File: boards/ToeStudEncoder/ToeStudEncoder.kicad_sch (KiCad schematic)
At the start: 23 parts, among them J1 Swell, J2 ISP, J3 ToeLeft, J4 ToeRight, J5 MIDI In, J6 Controller, J7 Pedal, J8 MIDI Out, U1 ATmega48-20P, U2 6N138

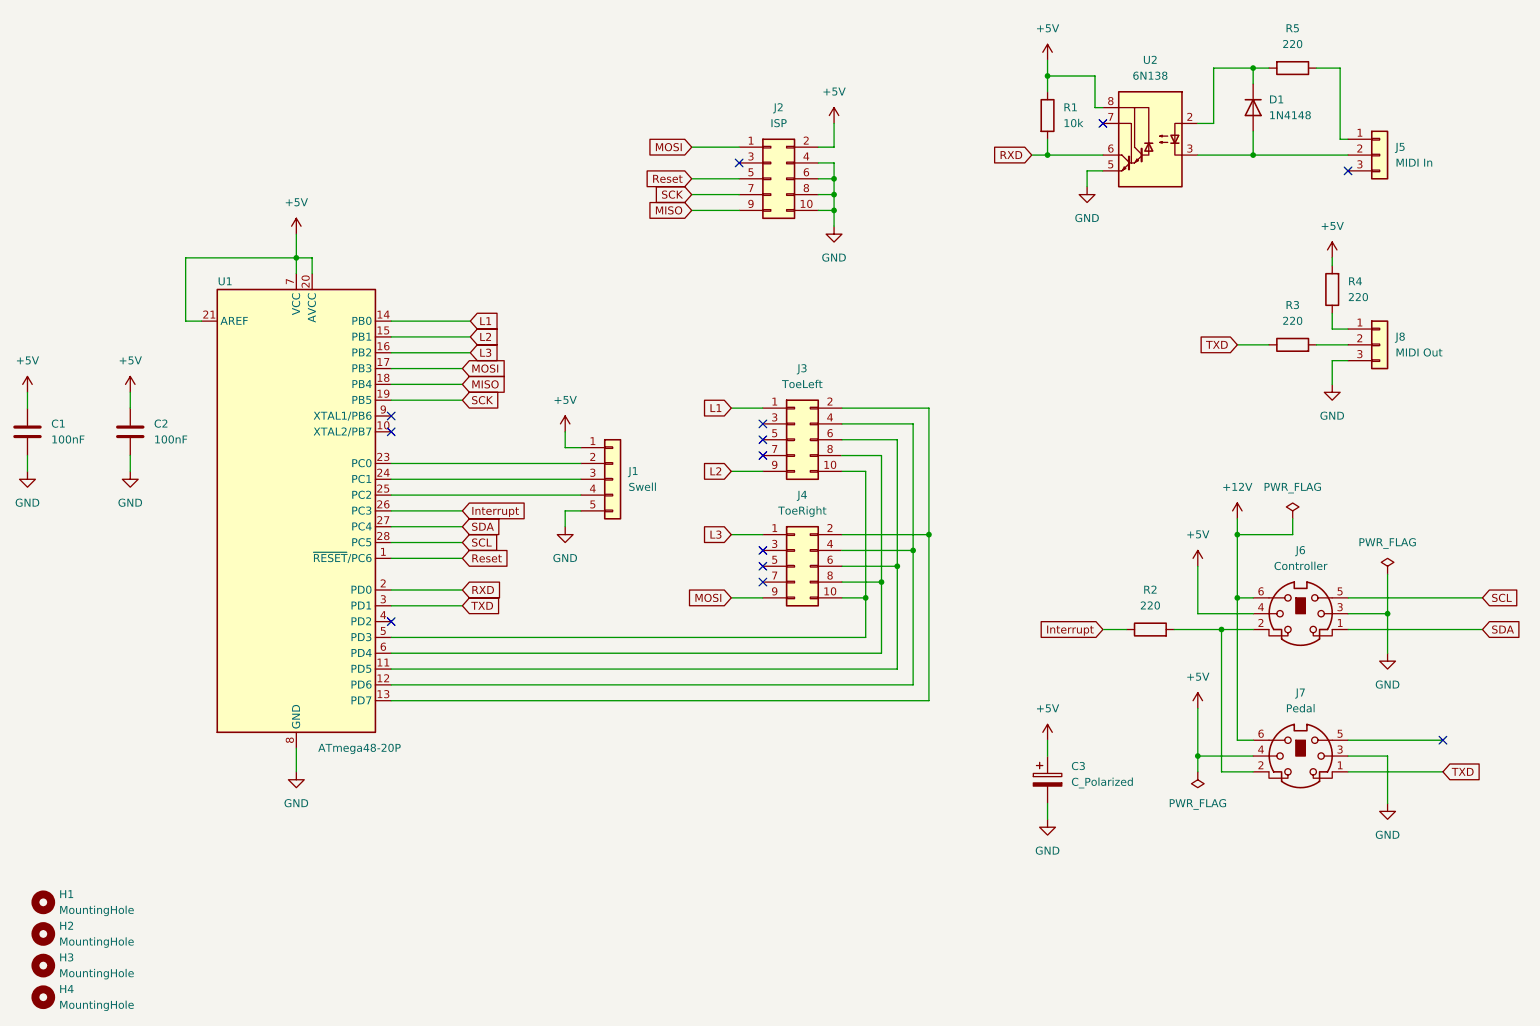
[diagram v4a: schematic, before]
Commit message: Updated to KiCAD 8, fixed optocouplers for MIDI and added powersupplies
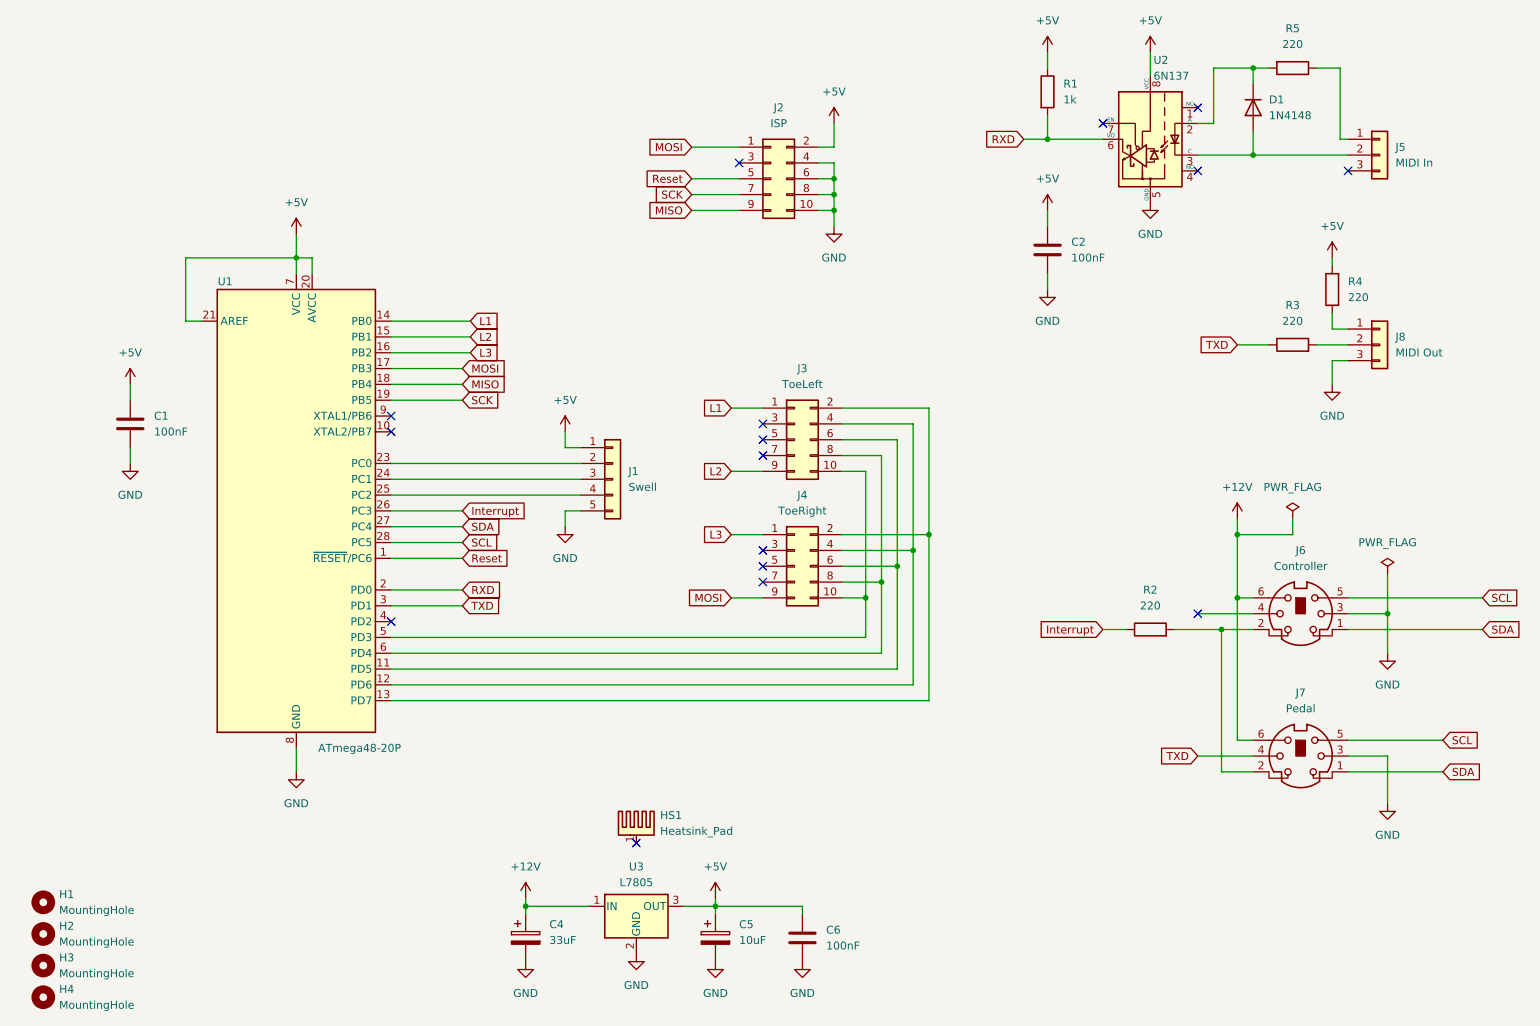
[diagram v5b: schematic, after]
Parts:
- removed C3: C_Polarized, Capacitor_THT:CP_Radial_D10.0mm_P5.00mm, symbol Device:C_Polarized
- removed U2: 6N138, Package_DIP:DIP-8_W7.62mm, symbol Isolator:6N138
- added C4: 33uF, Capacitor_THT:CP_Radial_D7.5mm_P2.50mm, symbol Device:C_Polarized
- added C5: 10uF, Capacitor_THT:CP_Radial_D6.3mm_P2.50mm, symbol Device:C_Polarized
- added C6: 100nF, Capacitor_THT:C_Disc_D4.3mm_W1.9mm_P5.00mm, symbol Device:C
- added HS1: Heatsink_Pad, Heatsink:Heatsink_AAVID_576802B03900G, symbol Mechanical:Heatsink_Pad
- added U2: 6N137, Package_DIP:DIP-8_W7.62mm, symbol Isolator:6N137
- added U3: L7805, Package_TO_SOT_THT:TO-220-3_Vertical, symbol Regulator_Linear:L7805
- R1: value 10k -> 1k
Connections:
- net +12V: now also C4.1, U3.1 (IN)
- net +5V: now also C5.1, C6.1, U2.8 (VCC), U3.3 (OUT); no longer J6.4, J7.4
- net GND: now also C4.2, C5.2, C6.2, U2.5 (GND), U3.2 (GND)
- net RXD: now also U2.6 (VO)
- net SCL: now also J7.5
- net SDA: now also J7.1
- net TXD: now also J7.4; no longer J7.1
- net at D1.2 (A), J5.2 (Pin_2): now also U2.3 (C)
- net at D1.1 (K), R5.2: now also U2.2 (A)
- no-connect marks 13 -> 16
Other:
- moved on the sheet: C1, C2, R1

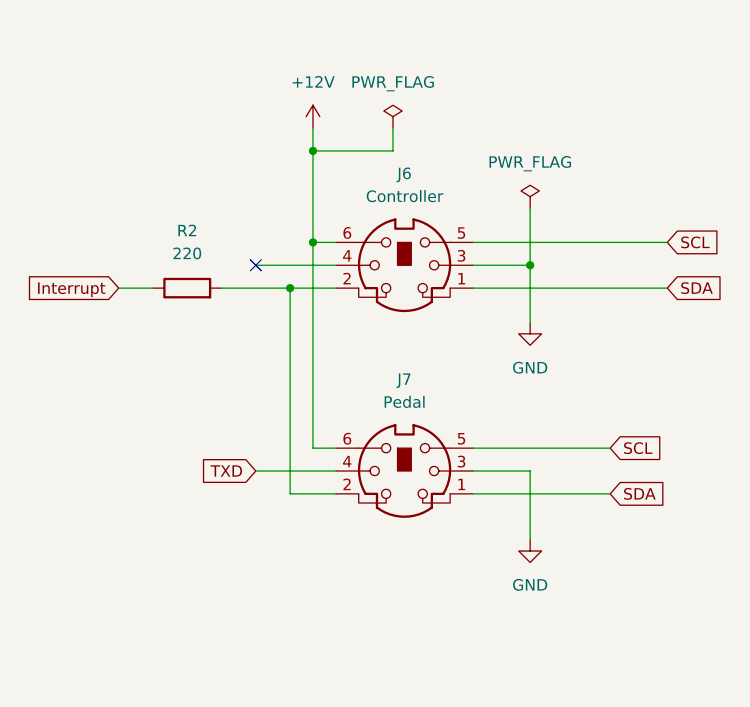
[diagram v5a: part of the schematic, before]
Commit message: Using custom TO220 cooler, fixed and finished several PCBs
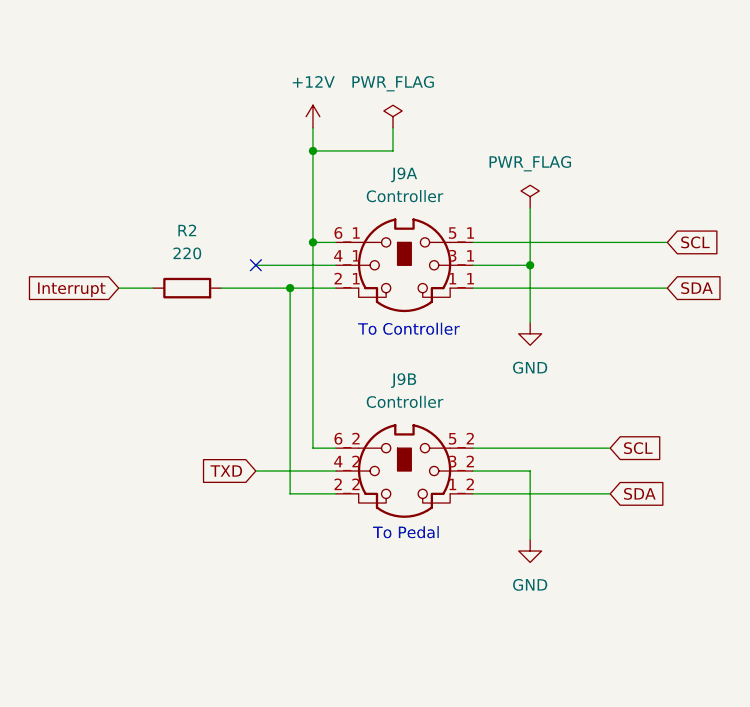
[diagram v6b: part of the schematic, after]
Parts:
- removed J6: Controller, symbol Connector:Mini-DIN-6
- removed J7: Pedal, symbol Connector:Mini-DIN-6
- added J9: Controller, SnapEDA:SWITCHCRAFT_DMD6FRA111, symbol Custom_Symbols:Mini-DIN-2x6
- HS1: footprint Heatsink:Heatsink_AAVID_576802B03900G -> Custom_Heatsinks:Heatsink_Aavid_TO-220_H12.7mm
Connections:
- net +12V: now also J9.6_1, J9.6_2
- net GND: now also J9.3_1, J9.3_2
- net SCL: now also J9.5_1, J9.5_2
- net SDA: now also J9.1_1, J9.1_2
- net TXD: now also J9.4_2
- net at R2.2: now also J9.2_1, J9.2_2
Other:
- note added: "To Controller"
- note added: "To Pedal"

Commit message: Finished PCB for ToeStudEncoder
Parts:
- R2, R3: footprint Resistor_THT:R_Axial_DIN0204_L3.6mm_D1.6mm_P2.54mm_Vertical -> Resistor_THT:R_Axial_DIN0204_L3.6mm_D1.6mm_P7.62mm_Horizontal
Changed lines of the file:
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@@
 			)
 		)
-		(property "Footprint" "Resistor_THT:R_Axial_DIN0204_L3.6mm_D1.6mm_P2.54mm_Vertical"
+		(property "Footprint" "Resistor_THT:R_Axial_DIN0204_L3.6mm_D1.6mm_P7.62mm_Horizontal"
 			(at 208.28 118.618 90)
 			(effects
@@
 			)
 		)
-		(property "Footprint" "Resistor_THT:R_Axial_DIN0204_L3.6mm_D1.6mm_P2.54mm_Vertical"
+		(property "Footprint" "Resistor_THT:R_Axial_DIN0204_L3.6mm_D1.6mm_P7.62mm_Horizontal"
 			(at 231.14 72.898 90)
 			(effects

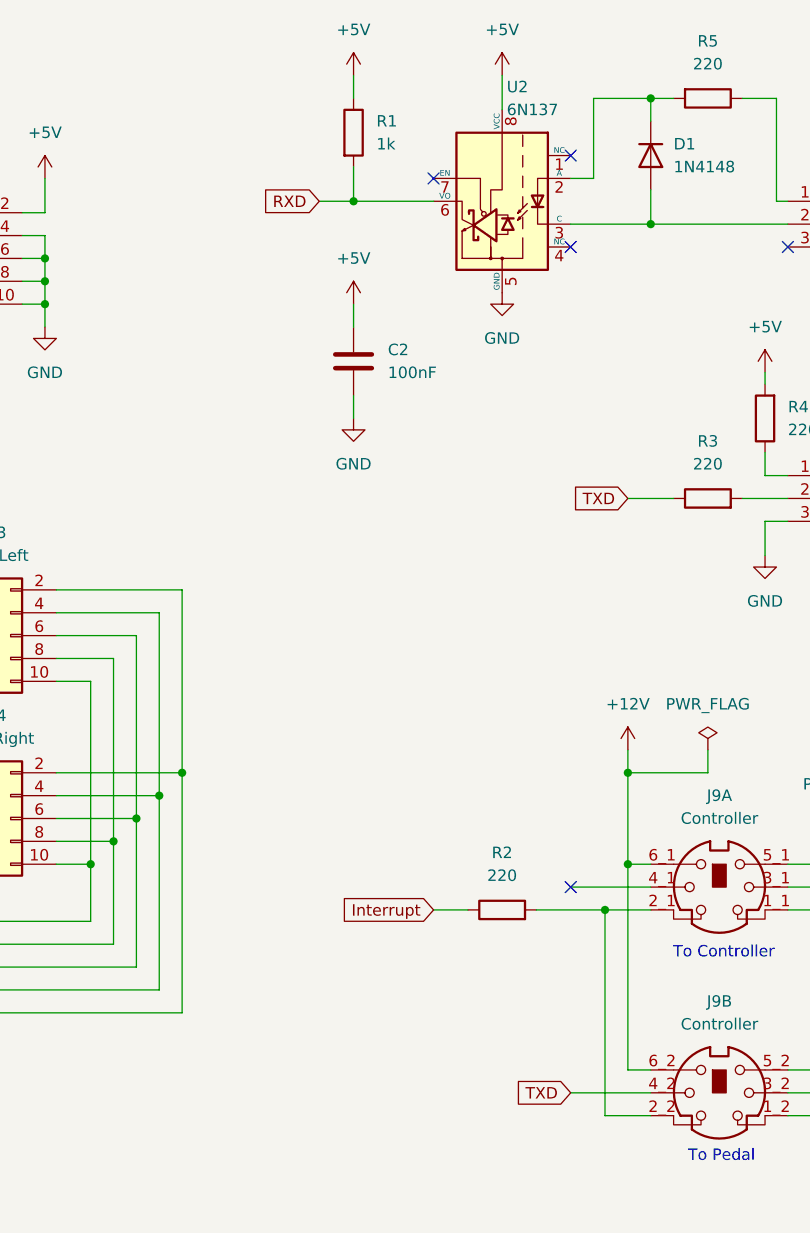
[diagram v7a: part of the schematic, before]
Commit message: Fixed interrupt line to use open collector, added pullups to I2C lines
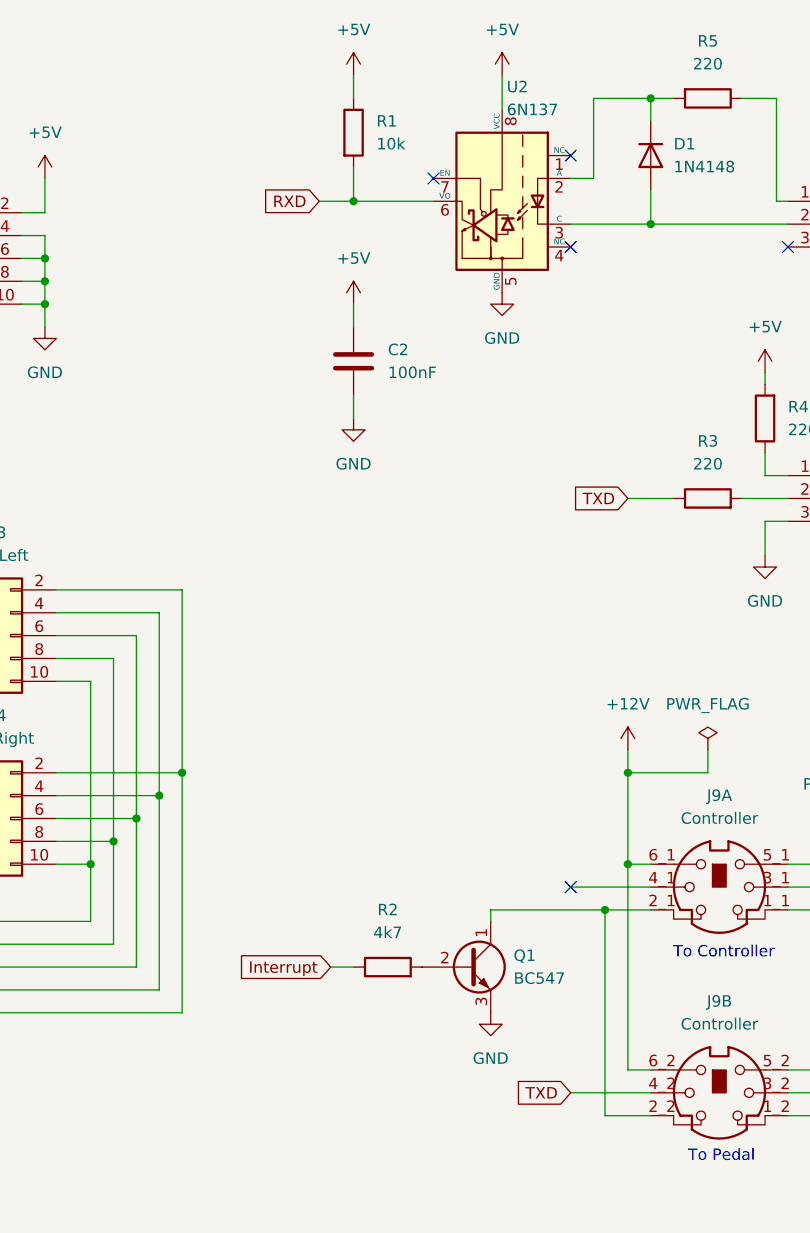
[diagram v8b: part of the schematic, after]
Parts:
- added Q1: BC547, Package_TO_SOT_THT:TO-92_Inline_Wide, symbol Transistor_BJT:BC547
- R1: value 1k -> 10k
- R2: value 220 -> 4k7
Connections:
- net GND: now also Q1.3 (E)
- net at J9.2_1, J9.2_2: now also Q1.1 (C); no longer R2.2
- new net: Q1.2 (B), R2.2
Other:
- moved on the sheet: R2
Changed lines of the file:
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@@
 	(wire
 		(pts
+			(xy 207.01 118.11) (xy 207.01 116.84)
+		)
+		(stroke
+			(width 0)
+			(type default)
+		)
+	)
+	(wire
+		(pts
 			(xy 238.76 38.1) (xy 238.76 26.67)
 		)
@@
 	(wire
 		(pts
-			(xy 200.66 116.84) (xy 204.47 116.84)
+			(xy 189.23 123.19) (xy 191.77 123.19)
 		)
 		(stroke
@@
 	(wire
 		(pts
-			(xy 212.09 116.84) (xy 219.71 116.84)
+			(xy 207.01 116.84) (xy 219.71 116.84)
 		)
 		(stroke
@@
 	(global_label "Interrupt"
 		(shape input)
-		(at 200.66 116.84 180)
+		(at 189.23 123.19 180)
 		(fields_autoplaced yes)
 		(effects
@@
 		)
 		(property "Intersheetrefs" "${INTERSHEET_REFS}"
-			(at 190.0826 116.7606 0)
+			(at 178.6526 123.1106 0)
 			(effects
 				(font
@@
 	)
 	(symbol
+		(lib_id "power:GND")
+		(at 207.01 128.27 0)
+		(unit 1)
+		(exclude_from_sim no)
+		(in_bom yes)
+		(on_board yes)
+		(dnp no)
+		(fields_autoplaced yes)
+		(property "Reference" "#PWR012"
+			(at 207.01 134.62 0)
+			(effects
+				(font
+					(size 1.27 1.27)
+				)
+				(hide yes)
+			)
+		)
+		(property "Value" "GND"
+			(at 207.01 133.35 0)
+			(effects
+				(font
+					(size 1.27 1.27)
+				)
+			)
+		)
+		(property "Footprint" ""
+			(at 207.01 128.27 0)
+			(effects
+				(font
+					(size 1.27 1.27)
+				)
+				(hide yes)
+			)
+		)
+		(property "Datasheet" ""
+			(at 207.01 128.27 0)
+			(effects
+				(font
+					(size 1.27 1.27)
+				)
+				(hide yes)
+			)
+		)
+		(property "Description" "Power symbol creates a global label with name \"GND\" , ground"
+			(at 207.01 128.27 0)
+			(effects
+				(font
+					(size 1.27 1.27)
+				)
+				(hide yes)
+			)
+		)
+		(pin "1"
+		)
+		(instances
+			(project "ToeStudEncoder"
+				(path "/a0f642fd-a17d-4032-8879-54d542360da8"
+					(reference "#PWR012")
+					(unit 1)
+				)
+			)
+		)
+	)
+	(symbol
+		(lib_id "Transistor_BJT:BC547")
+		(at 204.47 123.19 0)
+		(unit 1)
+		(exclude_from_sim no)
+		(in_bom yes)
+		(on_board yes)
+		(dnp no)
+		(fields_autoplaced yes)
+		(property "Reference" "Q1"
+			(at 209.55 121.9199 0)
+			(effects
+				(font
+					(size 1.27 1.27)
+				)
+				(justify left)
+			)
+		)
+		(property "Value" "BC547"
+			(at 209.55 124.4599 0)
+			(effects
+				(font
+					(size 1.27 1.27)
+				)
+				(justify left)
+			)
+		)
+		(property "Footprint" "Package_TO_SOT_THT:TO-92_Inline_Wide"
+			(at 209.55 125.095 0)
+			(effects
+				(font
+					(size 1.27 1.27)
+					(italic yes)
+				)
+				(justify left)
+				(hide yes)
+			)
+		)
+		(property "Datasheet" "https://www.onsemi.com/pub/Collateral/BC550-D.pdf"
+			(at 204.47 123.19 0)
+			(effects
+				(font
+					(size 1.27 1.27)
+				)
+				(justify left)
+				(hide yes)
+			)
+		)
+		(property "Description" "0.1A Ic, 45V Vce, Small Signal NPN Transistor, TO-92"
+			(at 204.47 123.19 0)
+			(effects
+				(font
+					(size 1.27 1.27)
+				)
+				(hide yes)
+			)
+		)
+		(pin "1"
+		)
+		(pin "2"
+		)
+		(pin "3"
+		)
+		(instances
+			(project "ToeStudEncoder"
+				(path "/a0f642fd-a17d-4032-8879-54d542360da8"
+					(reference "Q1")
+					(unit 1)
+				)
+			)
+		)
+	)
+	(symbol
 		(lib_id "power:PWR_FLAG")
 		(at 246.38 107.95 0)
@@
 	(symbol
 		(lib_id "Device:R")
-		(at 208.28 116.84 90)
+		(at 195.58 123.19 90)
 		(unit 1)
 		(exclude_from_sim no)
@@
 		(fields_autoplaced yes)
 		(property "Reference" "R2"
-			(at 208.28 110.49 90)
+			(at 195.58 116.84 90)
 			(effects
 				(font
@@
 			)
 		)
-		(property "Value" "220"
-			(at 208.28 113.03 90)
+		(property "Value" "4k7"
+			(at 195.58 119.38 90)
 			(effects
 				(font
@@
 		)
 		(property "Footprint" "Resistor_THT:R_Axial_DIN0204_L3.6mm_D1.6mm_P7.62mm_Horizontal"
-			(at 208.28 118.618 90)
+			(at 195.58 124.968 90)
 			(effects
 				(font
@@
 		)
 		(property "Datasheet" "~"
-			(at 208.28 116.84 0)
+			(at 195.58 123.19 0)
 			(effects
 				(font
@@
 		)
 		(property "Description" "Resistor"
-			(at 208.28 116.84 0)
+			(at 195.58 123.19 0)
 			(effects
 				(font
@@
 			)
 		)
-		(property "Value" "1k"
+		(property "Value" "10k"
 			(at 194.31 31.7499 0)
 			(effects
